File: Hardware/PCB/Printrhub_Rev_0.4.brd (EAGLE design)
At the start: 82.5 x 61.2 mm, 74 parts, among them J1 DM3D-SF, SW1 SPST_TACT-KMR2, SW2 SPST_TACT-KMR2, U1 MK20DX256VLH7, U2 AP1117E, U3 MAX308-SOT23, Y2 16Mhz/8pF

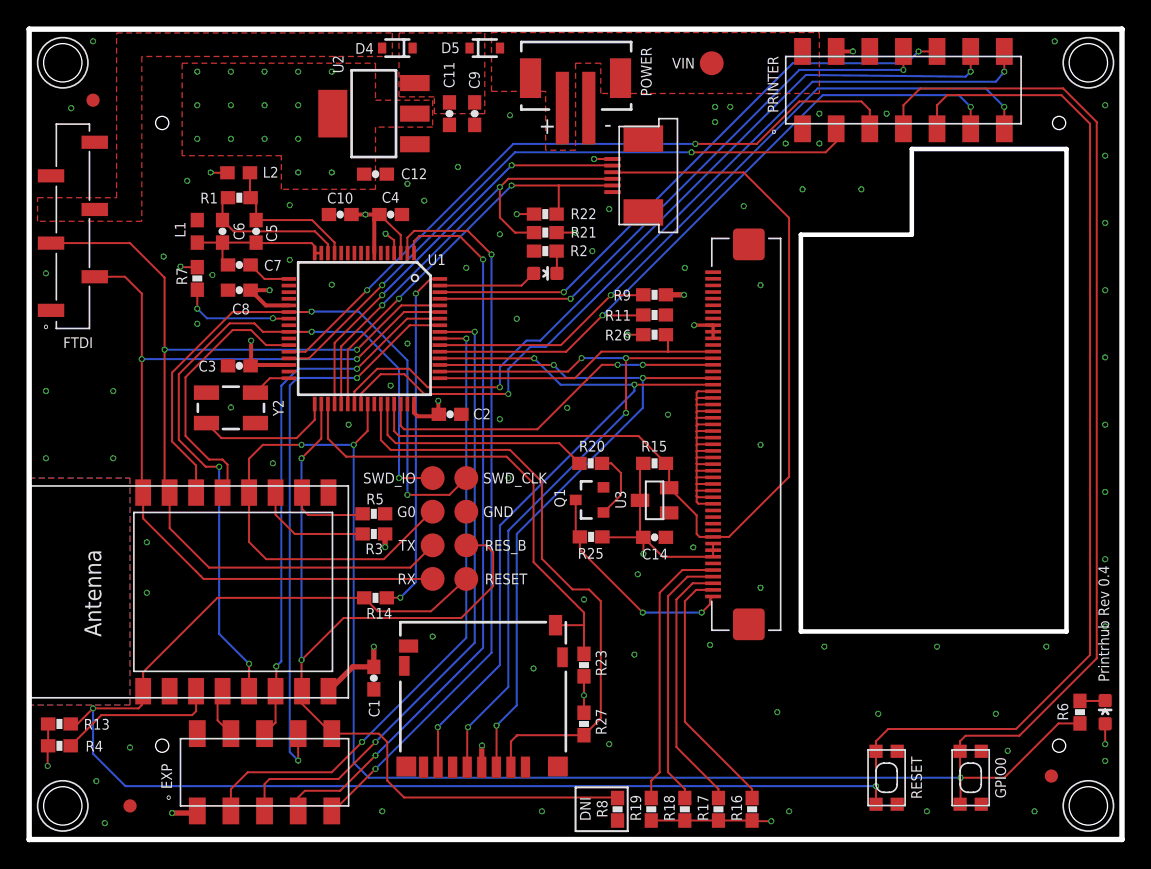
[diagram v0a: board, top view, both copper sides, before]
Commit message: Moved display 0.45mm to the right (from component side), moved some traces to make space and moved test points a bit to make them more centered above the SD card slot.
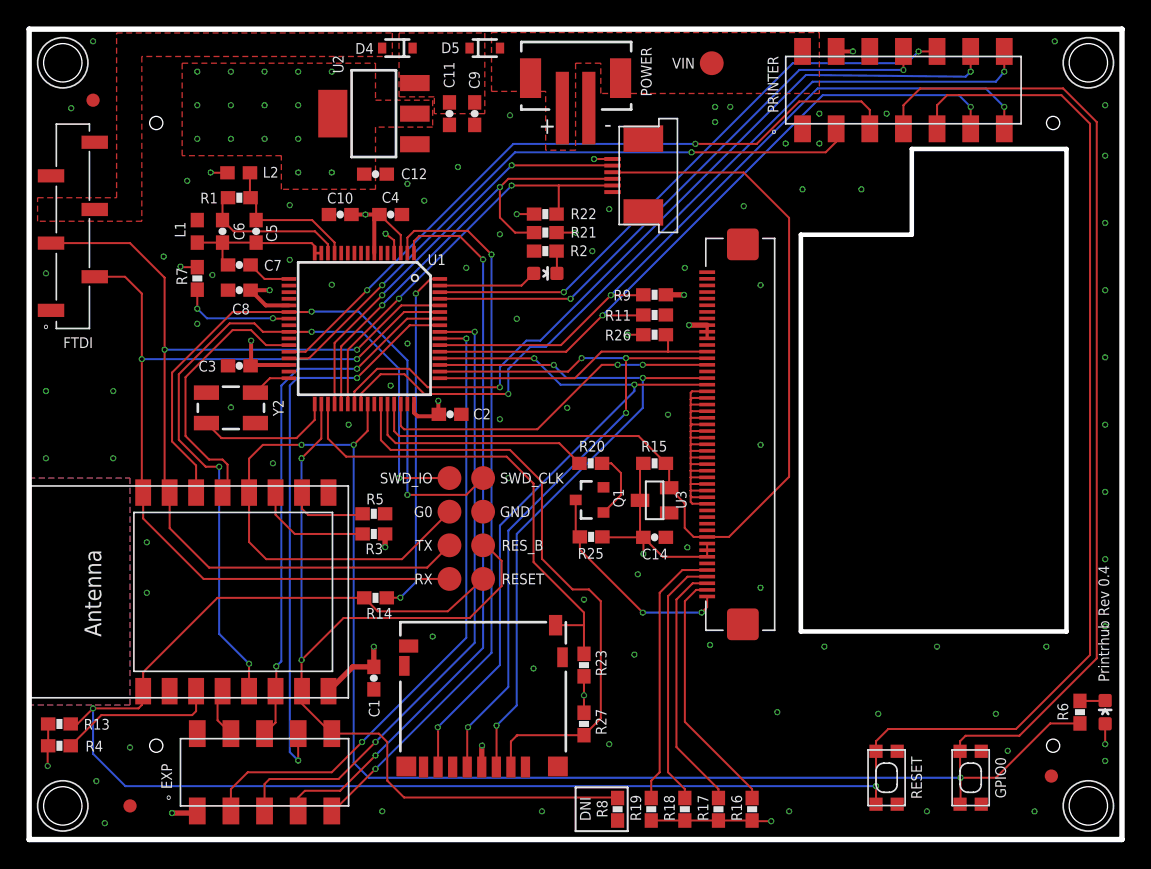
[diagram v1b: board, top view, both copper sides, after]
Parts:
- moved G0 1.27 mm to (31.8, 24.8)
- moved RX 1.27 mm to (31.8, 19.7)
- moved SWD_IO 1.27 mm to (31.8, 27.3)
- moved TX 1.27 mm to (31.8, 22.2)
- moved GND 1.27 mm to (34.3, 24.8)
- moved RESET 1.27 mm to (34.3, 19.7)
- moved RES_B 1.27 mm to (34.3, 22.2)
- moved SWD_CLK 1.27 mm to (34.3, 27.3)
- moved TFT1 0.45 mm to (40.8, 30.6)
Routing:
- net ESP_RESET: track 179.2 -> 180.5 mm
- net UART2_TX: track 73.2 -> 74.4 mm
- net SWD_IO: track 57.2 -> 58.5 mm
- net SWD_CLK: track 46.2 -> 47.4 mm
- net UART2_RX: track 69.3 -> 70.5 mm
- net ESP_GPIO0: track 191.8 -> 192.9 mm
- net N$17: track 31.1 -> 31.9 mm
- net 3.3V: track 79.9 -> 79.4 mm
